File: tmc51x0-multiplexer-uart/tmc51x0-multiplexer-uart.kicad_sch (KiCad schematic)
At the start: 0 parts

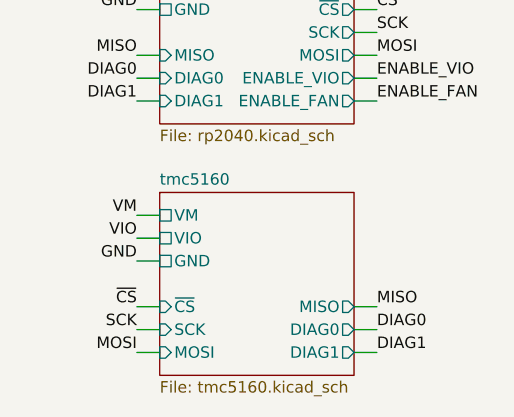
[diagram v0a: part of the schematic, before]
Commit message: Deleted unused schematics
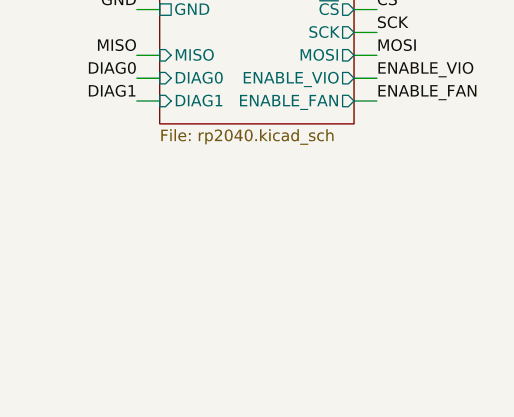
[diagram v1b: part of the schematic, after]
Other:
- removed sheet tmc5160
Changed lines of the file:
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@@
   (title_block
     (title "tmc51x0-multiplexer-uart")
-    (date "2024-05-10")
+    (date "2024-06-28")
     (rev "1.0")
     (company "Howard Hughes Medical Institute")
   )
   (wire (pts (xy 130.81 102.87) (xy 128.27 102.87))
-    (stroke (width 0) (type default))
-  )
-  (wire (pts (xy 130.81 128.27) (xy 128.27 128.27))
     (stroke (width 0) (type default))
   )
@@
     (stroke (width 0) (type default))
   )
-  (wire (pts (xy 128.27 118.11) (xy 130.81 118.11))
-    (stroke (width 0) (type default))
-  )
-  (wire (pts (xy 130.81 130.81) (xy 128.27 130.81))
-    (stroke (width 0) (type default))
-  )
   (wire (pts (xy 154.94 67.31) (xy 152.4 67.31))
-    (stroke (width 0) (type default))
-  )
-  (wire (pts (xy 130.81 125.73) (xy 128.27 125.73))
-    (stroke (width 0) (type default))
-  )
-  (wire (pts (xy 152.4 130.81) (xy 154.94 130.81))
     (stroke (width 0) (type default))
   )
@@
   )
   (wire (pts (xy 128.27 55.88) (xy 130.81 55.88))
-    (stroke (width 0) (type default))
-  )
-  (wire (pts (xy 128.27 115.57) (xy 130.81 115.57))
-    (stroke (width 0) (type default))
-  )
-  (wire (pts (xy 152.4 128.27) (xy 154.94 128.27))
-    (stroke (width 0) (type default))
-  )
-  (wire (pts (xy 152.4 125.73) (xy 154.94 125.73))
-    (stroke (width 0) (type default))
-  )
-  (wire (pts (xy 128.27 120.65) (xy 130.81 120.65))
     (stroke (width 0) (type default))
   )
@@
     (effects (font (size 1.27 1.27)) (justify left bottom))
   )
-  (label "DIAG1" (at 154.94 130.81 0) (fields_autoplaced)
-    (effects (font (size 1.27 1.27)) (justify left bottom))
-  )
   (label "VIO" (at 154.94 72.39 0) (fields_autoplaced)
     (effects (font (size 1.27 1.27)) (justify left bottom))
@@
   (label "+5V" (at 154.94 69.85 0) (fields_autoplaced)
     (effects (font (size 1.27 1.27)) (justify left bottom))
-  )
-  (label "MOSI" (at 128.27 130.81 180) (fields_autoplaced)
-    (effects (font (size 1.27 1.27)) (justify right bottom))
   )
   (label "ENABLE_VIO" (at 154.94 100.33 0) (fields_autoplaced)
@@
     (effects (font (size 1.27 1.27)) (justify right bottom))
   )
-  (label "VIO" (at 128.27 118.11 180) (fields_autoplaced)
-    (effects (font (size 1.27 1.27)) (justify right bottom))
-  )
-  (label "VM" (at 128.27 115.57 180) (fields_autoplaced)
-    (effects (font (size 1.27 1.27)) (justify right bottom))
-  )
   (label "SCK" (at 154.94 95.25 0) (fields_autoplaced)
-    (effects (font (size 1.27 1.27)) (justify left bottom))
-  )
-  (label "DIAG0" (at 154.94 128.27 0) (fields_autoplaced)
     (effects (font (size 1.27 1.27)) (justify left bottom))
   )
@@
     (effects (font (size 1.27 1.27)) (justify left bottom))
   )
-  (label "GND" (at 128.27 120.65 180) (fields_autoplaced)
-    (effects (font (size 1.27 1.27)) (justify right bottom))
-  )
-  (label "MISO" (at 154.94 125.73 0) (fields_autoplaced)
-    (effects (font (size 1.27 1.27)) (justify left bottom))
-  )
   (label "ENABLE_VIO" (at 128.27 72.39 180) (fields_autoplaced)
-    (effects (font (size 1.27 1.27)) (justify right bottom))
-  )
-  (label "SCK" (at 128.27 128.27 180) (fields_autoplaced)
     (effects (font (size 1.27 1.27)) (justify right bottom))
   )
   (label "~{CS}" (at 154.94 92.71 0) (fields_autoplaced)
     (effects (font (size 1.27 1.27)) (justify left bottom))
-  )
-  (label "~{CS}" (at 128.27 125.73 180) (fields_autoplaced)
-    (effects (font (size 1.27 1.27)) (justify right bottom))
   )
   (label "ENABLE_FAN" (at 128.27 74.93 180) (fields_autoplaced)
@@
     (effects (font (size 1.27 1.27)) (justify right bottom))
   )
-  (sheet (at 130.81 113.03) (size 21.59 20.32) (fields_autoplaced)
-    (stroke (width 0.1524) (type solid))
-    (fill (color 0 0 0 0.0000))
-    (property "Sheetname" "tmc5160" (at 130.81 112.3184 0)
-      (effects (font (size 1.27 1.27)) (justify left bottom))
-    )
-    (property "Sheetfile" "tmc5160.kicad_sch" (at 130.81 133.9346 0)
-      (effects (font (size 1.27 1.27)) (justify left top))
-    )
-    (pin "VM" passive (at 130.81 115.57 180)
-      (effects (font (size 1.27 1.27)) (justify left))
-    )
-    (pin "VIO" passive (at 130.81 118.11 180)
-      (effects (font (size 1.27 1.27)) (justify left))
-    )
-    (pin "GND" passive (at 130.81 120.65 180)
-      (effects (font (size 1.27 1.27)) (justify left))
-    )
-    (pin "~{CS}" input (at 130.81 125.73 180)
-      (effects (font (size 1.27 1.27)) (justify left))
-    )
-    (pin "SCK" input (at 130.81 128.27 180)
-      (effects (font (size 1.27 1.27)) (justify left))
-    )
-    (pin "DIAG0" output (at 152.4 128.27 0)
-      (effects (font (size 1.27 1.27)) (justify right))
-    )
-    (pin "DIAG1" output (at 152.4 130.81 0)
-      (effects (font (size 1.27 1.27)) (justify right))
-    )
-    (pin "MISO" output (at 152.4 125.73 0)
-      (effects (font (size 1.27 1.27)) (justify right))
-    )
-    (pin "MOSI" input (at 130.81 130.81 180)
-      (effects (font (size 1.27 1.27)) (justify left))
-    )
-    (instances
-      (project "tmc51x0-multiplexer-uart"
-        (path "/df2b2e89-e055-4140-95de-f1df723db034" (page "4"))
-      )
-    )
-  )
   (sheet (at 130.81 53.34) (size 21.59 5.08) (fields_autoplaced)

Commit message: Update components
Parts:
- added U101: MAX13431E, Janelia:21-0137I_T1033-1_MXM, symbol Janelia:MAX13431E
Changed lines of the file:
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@@
     (effects (font (size 1.27 1.27)) (justify right bottom))
+  )
+  (symbol (lib_id "Janelia:MAX13431E") (at 139.7 135.89 0) (unit 1)
+    (in_bom yes) (on_board yes) (dnp no) (fields_autoplaced)
+    (property "Reference" "U101" (at 141.8941 120.65 0)
+      (effects (font (size 1.27 1.27)) (justify left))
+    )
+    (property "Value" "MAX13431E" (at 141.8941 123.19 0)
+      (effects (font (size 1.27 1.27)) (justify left))
+    )
+    (property "Footprint" "Janelia:21-0137I_T1033-1_MXM" (at 139.7 153.67 0)
+      (effects (font (size 1.27 1.27)) hide)
+    )
+    (property "Datasheet" "" (at 139.7 134.62 0)
+      (effects (font (size 1.27 1.27)) hide)
+    )
+    (property "Synopsis" "IC TRANSCEIVER HALF 1/1" (at 139.7 135.89 0)
+      (effects (font (size 1.27 1.27)) hide)
+    )
+    (property "Manufacturer" "Analog Devices Inc./Maxim Integrated" (at 139.7 135.89 0)
+      (effects (font (size 1.27 1.27)) hide)
+    )
+    (property "Manufacturer Part Number" "MAX13431EETB+T" (at 139.7 135.89 0)
+      (effects (font (size 1.27 1.27)) hide)
+    )
+    (property "Vendor" "Digi-Key" (at 139.7 135.89 0)
+      (effects (font (size 1.27 1.27)) hide)
+    )
+    (property "Vendor Part Number" "MAX13431EETB+TCT-ND" (at 139.7 135.89 0)
+      (effects (font (size 1.27 1.27)) hide)
+    )
+    (property "LCSC" "C2672811" (at 139.7 135.89 0)
+      (effects (font (size 1.27 1.27)) hide)
+    )
+    (pin "8")
+    (pin "1")
+    (pin "4")
+    (pin "7")
+    (pin "6")
+    (pin "2")
+    (pin "5")
+    (pin "3")
+    (instances
+      (project "tmc51x0-multiplexer-uart"
+        (path "/df2b2e89-e055-4140-95de-f1df723db034"
+          (reference "U101") (unit 1)
+        )
+      )
+    )
   )
   (sheet (at 130.81 53.34) (size 21.59 5.08) (fields_autoplaced)

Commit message: Change sheets
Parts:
- removed U101: MAX13431E, Janelia:21-0137I_T1033-1_MXM, symbol Janelia:MAX13431E
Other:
- removed sheet rp2040
- added sheet microcontroller (microcontroller.kicad_sch)
- added sheet motor (motor.kicad_sch)
- sheet power ports: added ENABLE_VCC, VCC; removed ENABLE_FAN, ENABLE_VIO, VIO, VM
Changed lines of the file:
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@@
   (title_block
     (title "tmc51x0-multiplexer-uart")
-    (date "2024-06-28")
+    (date "2024-07-10")
     (rev "1.0")
     (company "Howard Hughes Medical Institute")
   )
-  (wire (pts (xy 130.81 102.87) (xy 128.27 102.87))
-    (stroke (width 0) (type default))
-  )
-  (wire (pts (xy 130.81 74.93) (xy 128.27 74.93))
-    (stroke (width 0) (type default))
-  )
   (wire (pts (xy 154.94 69.85) (xy 152.4 69.85))
-    (stroke (width 0) (type default))
-  )
-  (wire (pts (xy 152.4 97.79) (xy 154.94 97.79))
     (stroke (width 0) (type default))
   )
@@
     (stroke (width 0) (type default))
   )
-  (wire (pts (xy 130.81 97.79) (xy 128.27 97.79))
-    (stroke (width 0) (type default))
-  )
   (wire (pts (xy 128.27 55.88) (xy 130.81 55.88))
-    (stroke (width 0) (type default))
-  )
-  (wire (pts (xy 152.4 95.25) (xy 154.94 95.25))
-    (stroke (width 0) (type default))
-  )
-  (wire (pts (xy 130.81 100.33) (xy 128.27 100.33))
-    (stroke (width 0) (type default))
-  )
-  (wire (pts (xy 154.94 74.93) (xy 152.4 74.93))
-    (stroke (width 0) (type default))
-  )
-  (wire (pts (xy 152.4 102.87) (xy 154.94 102.87))
-    (stroke (width 0) (type default))
-  )
-  (wire (pts (xy 128.27 90.17) (xy 130.81 90.17))
-    (stroke (width 0) (type default))
-  )
-  (wire (pts (xy 128.27 92.71) (xy 130.81 92.71))
-    (stroke (width 0) (type default))
-  )
-  (wire (pts (xy 152.4 100.33) (xy 154.94 100.33))
     (stroke (width 0) (type default))
   )
@@
     (stroke (width 0) (type default))
   )
-  (wire (pts (xy 152.4 92.71) (xy 154.94 92.71))
-    (stroke (width 0) (type default))
-  )
   (wire (pts (xy 130.81 72.39) (xy 128.27 72.39))
     (stroke (width 0) (type default))
   )
-  (label "GND" (at 154.94 74.93 0) (fields_autoplaced)
+  (label "GND" (at 154.94 72.39 0) (fields_autoplaced)
     (effects (font (size 1.27 1.27)) (justify left bottom))
-  )
-  (label "VIO" (at 154.94 72.39 0) (fields_autoplaced)
-    (effects (font (size 1.27 1.27)) (justify left bottom))
-  )
-  (label "DIAG1" (at 128.27 102.87 180) (fields_autoplaced)
-    (effects (font (size 1.27 1.27)) (justify right bottom))
   )
   (label "+5V" (at 154.94 69.85 0) (fields_autoplaced)
     (effects (font (size 1.27 1.27)) (justify left bottom))
   )
-  (label "ENABLE_VIO" (at 154.94 100.33 0) (fields_autoplaced)
-    (effects (font (size 1.27 1.27)) (justify left bottom))
-  )
-  (label "MISO" (at 128.27 97.79 180) (fields_autoplaced)
-    (effects (font (size 1.27 1.27)) (justify right bottom))
-  )
-  (label "ENABLE_FAN" (at 154.94 102.87 0) (fields_autoplaced)
-    (effects (font (size 1.27 1.27)) (justify left bottom))
-  )
-  (label "+5V" (at 128.27 90.17 180) (fields_autoplaced)
-    (effects (font (size 1.27 1.27)) (justify right bottom))
-  )
-  (label "SCK" (at 154.94 95.25 0) (fields_autoplaced)
-    (effects (font (size 1.27 1.27)) (justify left bottom))
-  )
-  (label "GND" (at 128.27 92.71 180) (fields_autoplaced)
-    (effects (font (size 1.27 1.27)) (justify right bottom))
-  )
   (label "GND" (at 128.27 55.88 180) (fields_autoplaced)
     (effects (font (size 1.27 1.27)) (justify right bottom))
   )
-  (label "MOSI" (at 154.94 97.79 0) (fields_autoplaced)
-    (effects (font (size 1.27 1.27)) (justify left bottom))
-  )
-  (label "ENABLE_VIO" (at 128.27 72.39 180) (fields_autoplaced)
+  (label "ENABLE_VCC" (at 128.27 72.39 180) (fields_autoplaced)
     (effects (font (size 1.27 1.27)) (justify right bottom))
   )
-  (label "~{CS}" (at 154.94 92.71 0) (fields_autoplaced)
+  (label "VCC" (at 154.94 67.31 0) (fields_autoplaced)
     (effects (font (size 1.27 1.27)) (justify left bottom))
-  )
-  (label "ENABLE_FAN" (at 128.27 74.93 180) (fields_autoplaced)
-    (effects (font (size 1.27 1.27)) (justify right bottom))
-  )
-  (label "VM" (at 154.94 67.31 0) (fields_autoplaced)
-    (effects (font (size 1.27 1.27)) (justify left bottom))
-  )
-  (label "DIAG0" (at 128.27 100.33 180) (fields_autoplaced)
-    (effects (font (size 1.27 1.27)) (justify right bottom))
-  )
-  (symbol (lib_id "Janelia:MAX13431E") (at 139.7 135.89 0) (unit 1)
-    (in_bom yes) (on_board yes) (dnp no) (fields_autoplaced)
-    (property "Reference" "U101" (at 141.8941 120.65 0)
-      (effects (font (size 1.27 1.27)) (justify left))
-    )
-    (property "Value" "MAX13431E" (at 141.8941 123.19 0)
-      (effects (font (size 1.27 1.27)) (justify left))
-    )
-    (property "Footprint" "Janelia:21-0137I_T1033-1_MXM" (at 139.7 153.67 0)
-      (effects (font (size 1.27 1.27)) hide)
-    )
-    (property "Datasheet" "" (at 139.7 134.62 0)
-      (effects (font (size 1.27 1.27)) hide)
-    )
-    (property "Synopsis" "IC TRANSCEIVER HALF 1/1" (at 139.7 135.89 0)
-      (effects (font (size 1.27 1.27)) hide)
-    )
-    (property "Manufacturer" "Analog Devices Inc./Maxim Integrated" (at 139.7 135.89 0)
-      (effects (font (size 1.27 1.27)) hide)
-    )
-    (property "Manufacturer Part Number" "MAX13431EETB+T" (at 139.7 135.89 0)
-      (effects (font (size 1.27 1.27)) hide)
-    )
-    (property "Vendor" "Digi-Key" (at 139.7 135.89 0)
-      (effects (font (size 1.27 1.27)) hide)
-    )
-    (property "Vendor Part Number" "MAX13431EETB+TCT-ND" (at 139.7 135.89 0)
-      (effects (font (size 1.27 1.27)) hide)
-    )
-    (property "LCSC" "C2672811" (at 139.7 135.89 0)
-      (effects (font (size 1.27 1.27)) hide)
-    )
-    (pin "8")
-    (pin "1")
-    (pin "4")
-    (pin "7")
-    (pin "6")
-    (pin "2")
-    (pin "5")
-    (pin "3")
-    (instances
-      (project "tmc51x0-multiplexer-uart"
-        (path "/df2b2e89-e055-4140-95de-f1df723db034"
-          (reference "U101") (unit 1)
-        )
-      )
-    )
   )
   (sheet (at 130.81 53.34) (size 21.59 5.08) (fields_autoplaced)
@@
     )
   )
-  (sheet (at 130.81 87.63) (size 21.59 17.78) (fields_autoplaced)
+  (sheet (at 130.81 121.92) (size 21.59 15.24) (fields_autoplaced)
     (stroke (width 0.1524) (type solid))
     (fill (color 0 0 0 0.0000))
-    (property "Sheetname" "rp2040" (at 130.81 86.9184 0)
+    (property "Sheetname" "motor" (at 130.81 121.2084 0)
       (effects (font (size 1.27 1.27)) (justify left bottom))
     )
-    (property "Sheetfile" "rp2040.kicad_sch" (at 130.81 105.9946 0)
+    (property "Sheetfile" "motor.kicad_sch" (at 130.81 137.7446 0)
       (effects (font (size 1.27 1.27)) (justify left top))
-    )
-    (pin "GND" passive (at 130.81 92.71 180)
-      (effects (font (size 1.27 1.27)) (justify left))
-    )
-    (pin "SCK" output (at 152.4 95.25 0)
-      (effects (font (size 1.27 1.27)) (justify right))
-    )
-    (pin "~{CS}" output (at 152.4 92.71 0)
-      (effects (font (size 1.27 1.27)) (justify right))
-    )
-    (pin "MOSI" output (at 152.4 97.79 0)
-      (effects (font (size 1.27 1.27)) (justify right))
-    )
-    (pin "MISO" input (at 130.81 97.79 180)
-      (effects (font (size 1.27 1.27)) (justify left))
-    )
-    (pin "DIAG0" input (at 130.81 100.33 180)
-      (effects (font (size 1.27 1.27)) (justify left))
-    )
-    (pin "DIAG1" input (at 130.81 102.87 180)
-      (effects (font (size 1.27 1.27)) (justify left))
-    )
-    (pin "ENABLE_VIO" output (at 152.4 100.33 0)
-      (effects (font (size 1.27 1.27)) (justify right))
-    )
-    (pin "ENABLE_FAN" output (at 152.4 102.87 0)
-      (effects (font (size 1.27 1.27)) (justify right))
-    )
-    (pin "+5V" passive (at 130.81 90.17 180)
-      (effects (font (size 1.27 1.27)) (justify left))
     )
     (instances
       (project "tmc51x0-multiplexer-uart"
-        (path "/df2b2e89-e055-4140-95de-f1df723db034" (page "13"))
+        (path "/df2b2e89-e055-4140-95de-f1df723db034" (page "5"))
       )
     )
   )
-  (sheet (at 130.81 64.77) (size 21.59 12.7) (fields_autoplaced)
+  (sheet (at 130.81 83.82) (size 21.59 29.21) (fields_autoplaced)
+    (stroke (width 0.1524) (type solid))
+    (fill (color 0 0 0 0.0000))
+    (property "Sheetname" "microcontroller" (at 130.81 83.1084 0)
+      (effects (font (size 1.27 1.27)) (justify left bottom))
+    )
+    (property "Sheetfile" "microcontroller.kicad_sch" (at 130.81 113.6146 0)
+      (effects (font (size 1.27 1.27)) (justify left top))
+    )
+    (instances
+      (project "tmc51x0-multiplexer-uart"
+        (path "/df2b2e89-e055-4140-95de-f1df723db034" (page "4"))
+      )
+    )
+  )
+  (sheet (at 130.81 64.77) (size 21.59 10.16) (fields_autoplaced)
     (stroke (width 0.1524) (type solid))
     (fill (color 0 0 0 0.0000))
@@
       (effects (font (size 1.27 1.27)) (justify left bottom))
     )
-    (property "Sheetfile" "power.kicad_sch" (at 130.81 78.0546 0)
+    (property "Sheetfile" "power.kicad_sch" (at 130.81 75.5146 0)
       (effects (font (size 1.27 1.27)) (justify left top))
     )
-    (pin "GND" passive (at 152.4 74.93 0)
+    (pin "GND" passive (at 152.4 72.39 0)
       (effects (font (size 1.27 1.27)) (justify right))
-    )
-    (pin "VM" passive (at 152.4 67.31 0)
-      (effects (font (size 1.27 1.27)) (justify right))
-    )
-    (pin "VIO" passive (at 152.4 72.39 0)
-      (effects (font (size 1.27 1.27)) (justify right))
-    )
-    (pin "ENABLE_VIO" input (at 130.81 72.39 180)
-      (effects (font (size 1.27 1.27)) (justify left))
-    )
-    (pin "ENABLE_FAN" input (at 130.81 74.93 180)
-      (effects (font (size 1.27 1.27)) (justify left))
     )
     (pin "+5V" passive (at 152.4 69.85 0)
       (effects (font (size 1.27 1.27)) (justify right))
     )
+    (pin "ENABLE_VCC" input (at 130.81 72.39 180)
+      (effects (font (size 1.27 1.27)) (justify left))
+    )
+    (pin "VCC" passive (at 152.4 67.31 0)
+      (effects (font (size 1.27 1.27)) (justify right))
+    )

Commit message: Add components
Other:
- sheet motor renamed motor0
- added sheet motor1 (motor.kicad_sch)
- added sheet motor2 (motor.kicad_sch)
- added sheet motor3 (motor.kicad_sch)
- added sheet motor4 (motor.kicad_sch)
- added sheet motor5 (motor.kicad_sch)
- added sheet motor6 (motor.kicad_sch)
- sheet microcontroller ports: added +3.3V, +5V, ENABLE_TX_0, ENABLE_TX_1, ENABLE_TX_2, ENABLE_TX_3, ENABLE_TX_4, ENABLE_TX_5, ENABLE_TX_6, ENABLE_TX_7, GND, RX, TX, VCC_ENABLE, ~{ENABLE_RX_0}, ~{ENABLE_RX_1}, ~{ENABLE_RX_2}, ~{ENABLE_RX_3}, ~{ENABLE_RX_4}, ~{ENABLE_RX_5}, ~{ENABLE_RX_6}, ~{ENABLE_RX_7}; removed none
- sheet motor0 ports: added +3.3V, +5V, ENABLE_TX, GND, RX, TX, VAA, ~{ENABLE_RX}; removed none
